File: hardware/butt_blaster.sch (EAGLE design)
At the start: 6 parts

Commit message: more butts
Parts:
- added L1: (no value), A_butts:INDUCTORAXIAL-PTH-7.68MM
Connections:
- new net 5V: U1.VBUS
- new net GND: U1.GND
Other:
- moved on the sheet: LED1, LED2, LED3
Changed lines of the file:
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@@
 <setting verticaltext="up"/>
 </settings>
-<grid distance="100" unitdist="mil" unit="mil" style="lines" multiple="1" display="yes" altdistance="2" altunitdist="mil" altunit="mil"/>
+<grid distance="100" unitdist="mil" unit="mil" style="lines" multiple="1" display="yes" altdistance="1" altunitdist="mil" altunit="mil"/>
 <layers>
 <layer number="1" name="Top" color="4" fill="1" visible="no" active="no"/>
@@
 <part name="LED2" library="A_butts" deviceset="LED" device="5MM_SHORTPADS"/>
 <part name="LED3" library="A_butts" deviceset="LED" device="5MM_SHORTPADS"/>
+<part name="SUPPLY1" library="A_butts" deviceset="5V" device=""/>
+<part name="SUPPLY2" library="A_butts" deviceset="5V" device=""/>
+<part name="GND1" library="A_butts" deviceset="GND" device=""/>
+<part name="GND2" library="A_butts" deviceset="GND" device=""/>
+<part name="L1" library="A_butts" deviceset="INDUCTOR" device="AXIAL-PTH-7.68MM"/>
 </parts>
 <sheets>
@@
 <instance part="H1" gate="G$1" x="10.16" y="93.98"/>
 <instance part="H2" gate="G$1" x="15.24" y="93.98"/>
-<instance part="LED1" gate="G$1" x="63.5" y="68.58"/>
-<instance part="LED2" gate="G$1" x="73.66" y="68.58"/>
-<instance part="LED3" gate="G$1" x="83.82" y="68.58"/>
+<instance part="LED1" gate="G$1" x="40.64" y="71.12"/>
+<instance part="LED2" gate="G$1" x="48.26" y="71.12"/>
+<instance part="LED3" gate="G$1" x="55.88" y="71.12"/>
+<instance part="SUPPLY1" gate="G$1" x="22.86" y="76.2"/>
+<instance part="SUPPLY2" gate="G$1" x="40.64" y="91.44"/>
+<instance part="GND1" gate="1" x="22.86" y="58.42"/>
+<instance part="GND2" gate="1" x="48.26" y="53.34"/>
+<instance part="L1" gate="G$1" x="76.2" y="81.28"/>
 </instances>
 <busses>
 </busses>
 <nets>
+<net name="5V" class="0">
+<segment>
+<pinref part="U1" gate="G$1" pin="VBUS"/>
+<wire x1="20.32" y1="73.66" x2="22.86" y2="73.66" width="0.1524" layer="91"/>
+<wire x1="22.86" y1="73.66" x2="22.86" y2="76.2" width="0.1524" layer="91"/>
+<pinref part="SUPPLY1" gate="G$1" pin="5V"/>
+</segment>
+</net>
+<net name="GND" class="0">
+<segment>
+<pinref part="U1" gate="G$1" pin="GND"/>
+<wire x1="20.32" y1="63.5" x2="22.86" y2="63.5" width="0.1524" layer="91"/>
+<wire x1="22.86" y1="63.5" x2="22.86" y2="60.96" width="0.1524" layer="91"/>
+<pinref part="GND1" gate="1" pin="GND"/>
+</segment>
+</net>
 </nets>
 </sheet>

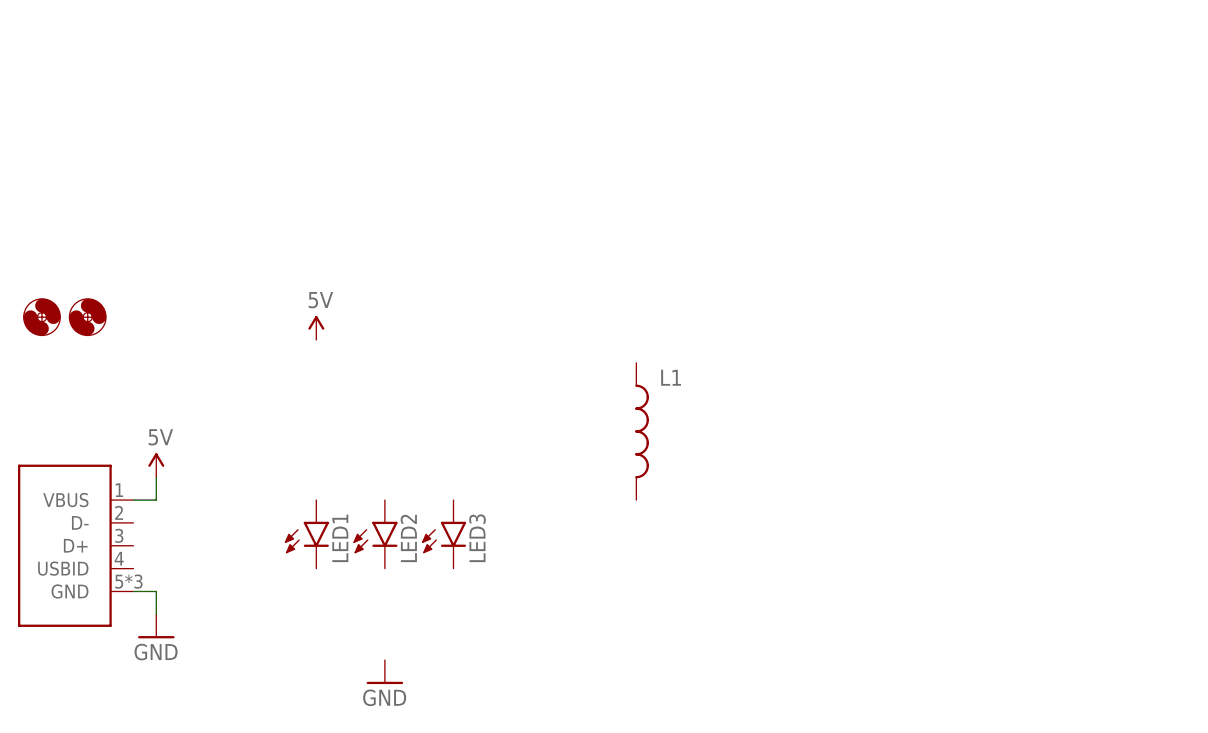
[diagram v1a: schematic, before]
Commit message: basing this on a AC/DC LED driver
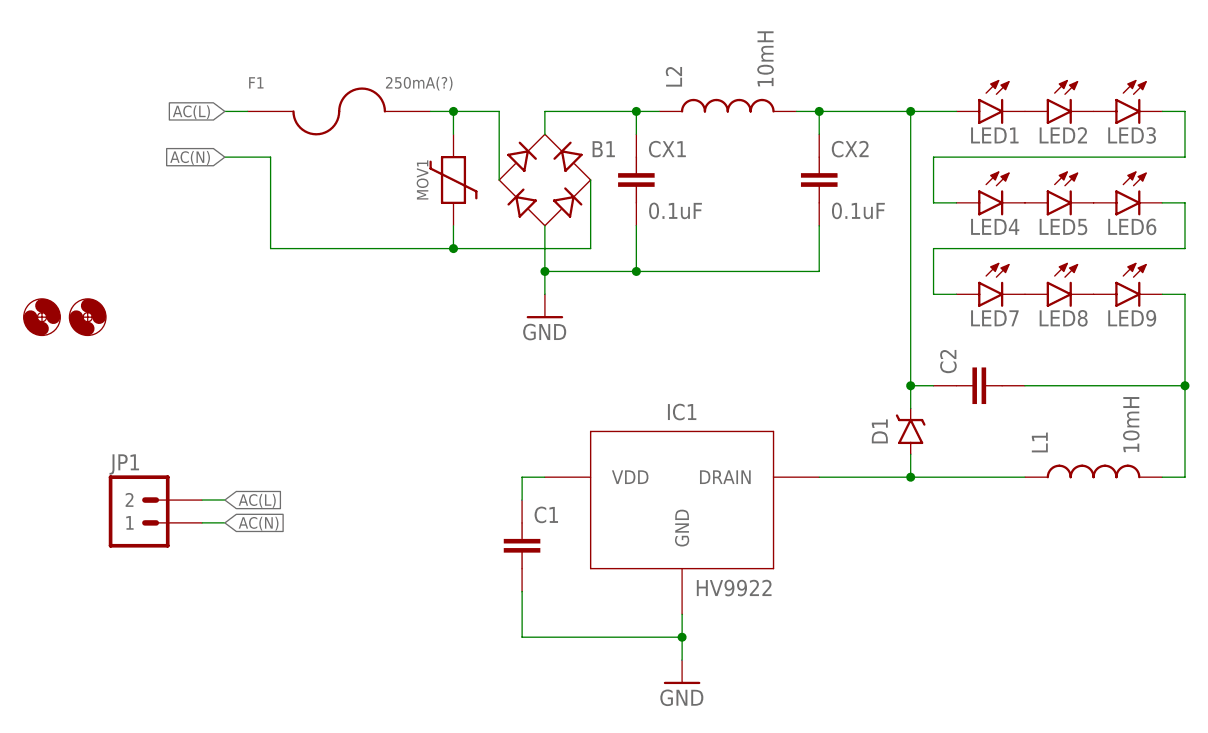
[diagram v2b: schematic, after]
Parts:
- removed U1: (no value), A_butts:USB-ABCOMBO
- added B1: (no value), A_butts:RB1ANOSUCK
- added C1, C2: (no value), A_butts:CAPACITOR-CERAMIC025-024X044
- added CX1, CX2: 0.1uF, A_butts:CXXC10B5
- added D1: (no value), A_butts:DIODE-SCHOTTKYPTH-7.68MM
- added F1: 250mA(?), A_butts:FUSETR5
- added IC1: HV9922, A_butts:HV9922
- added JP1: M025MM, A_butts:M025MM
- added L2: 10mH, A_butts:INDUCTORAXIAL-PTH-10.16MM
- added LED4, LED5, LED6, LED7, LED8, LED9: LED5MM_SHORTPADS, A_butts:LED5MM_SHORTPADS
- added MOV1: (no value), A_butts:VARISITORVAR-5.08MM-PTH
- L1: value (none) -> 10mH; device A_butts:INDUCTORAXIAL-PTH-7.68MM -> A_butts:INDUCTORRLB0912
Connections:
- removed net 5V: U1.VBUS
- new net AC(L): F1.1, JP1.2
- new net AC(N): B1.AC2, JP1.1, MOV1.P$1
- new net N$1: LED1.C, LED2.A
- new net N$10: D1.A, IC1.DRAIN, L1.1
- new net N$11: C2.1, CX2.1, D1.C, L2.2, LED1.A
- new net N$12: B1.AC1, F1.2, MOV1.P$2
- new net N$13: B1.+, CX1.1, L2.1
- new net N$14: C1.1, IC1.VDD
- new net N$2: LED2.C, LED3.A
- new net N$3: LED4.C, LED5.A
- new net N$4: LED5.C, LED6.A
- new net N$5: LED3.C, LED4.A
- new net N$6: LED6.C, LED7.A
- new net N$7: LED7.C, LED8.A
- new net N$8: LED8.C, LED9.A
- new net N$9: C2.2, L1.2, LED9.C
- net GND: now also B1.-, C1.2, CX1.2, CX2.2, IC1.GND; no longer U1.GND
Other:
- moved on the sheet: L1, LED1, LED2, LED3
